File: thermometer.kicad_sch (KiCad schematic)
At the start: 3 parts, among them J1 Conn_01x07, U1 MCP9600-E_MX

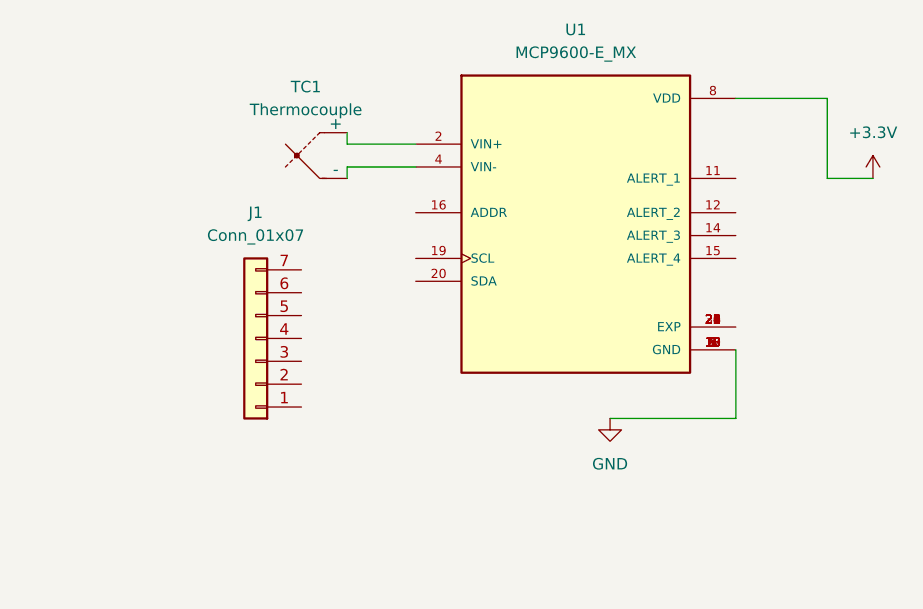
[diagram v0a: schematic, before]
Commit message: Update: Added bmp581 Pressure Sensor to temperature sensor daughter board.
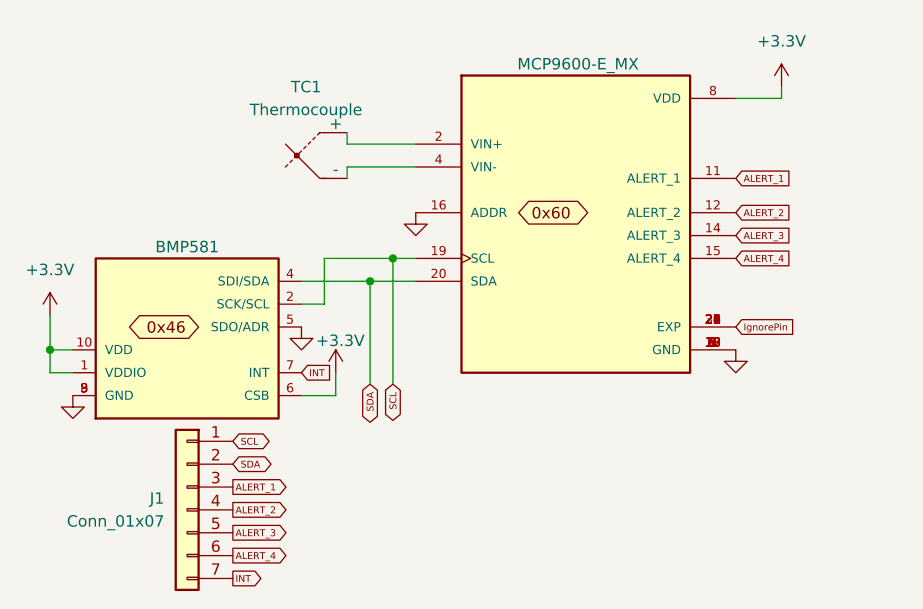
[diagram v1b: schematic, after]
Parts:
- added U2: BMP581, BMP581:BMP581, symbol BMP581:BMP581
- J1: footprint Connector_PinHeader_1.00mm:PinHeader_1x07_P1.00mm_Vertical -> (none)
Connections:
- net +3.3V: now also U2.1 (VDDIO), U2.10 (VDD), U2.6 (CSB)
- net GND: now also U1.16 (ADDR), U2.3 (GND), U2.5 (SDO/ADR), U2.8 (GND), U2.9 (GND)
- net SCL: now reaches J1.1 (Pin_1)
- net SCL: now also U1.19 (SCL), U2.2 (SCK/SCL)
- net SDA: now reaches J1.2 (Pin_2)
- net SDA: now also U1.20 (SDA), U2.4 (SDI/SDA)
- net ALERT_1: now reaches J1.3 (Pin_3)
- net ALERT_1: now also U1.11 (ALERT_1)
- net ALERT_2: now reaches J1.4 (Pin_4)
- net ALERT_2: now also U1.12 (ALERT_2)
- net ALERT_3: now reaches J1.5 (Pin_5)
- net ALERT_3: now also U1.14 (ALERT_3)
- net ALERT_4: now reaches J1.6 (Pin_6)
- net ALERT_4: now also U1.15 (ALERT_4)
- net INT: now reaches J1.7 (Pin_7)
- net INT: now also U2.7 (INT)
- net IgnorePin: now reaches U1.21 (EXP), U1.22 (EXP), U1.23 (EXP), U1.24 (EXP), U1.25 (EXP), U1.26 (EXP), U1.27 (EXP), U1.28 (EXP), U1.29 (EXP), U1.30 (EXP)
